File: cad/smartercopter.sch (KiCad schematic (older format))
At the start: 26 parts, among them P1 CONN_5, U1 CC2541, X1 32Mhz

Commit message: everything has a footprint
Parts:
- P1: footprint (none) -> Pin_Arrays:pin_array_1x05
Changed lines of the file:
@@
 F 0 "P1" H 5900 5650 50  0000 C CNN
 F 1 "CONN_5" V 6000 5350 50  0000 C CNN
-F 2 "" H 5900 5350 60  0001 C CNN
+F 2 "Pin_Arrays:pin_array_1x05" H 5900 5350 60  0001 C CNN
 F 3 "" H 5900 5350 60  0000 C CNN
 	1    5900 5350

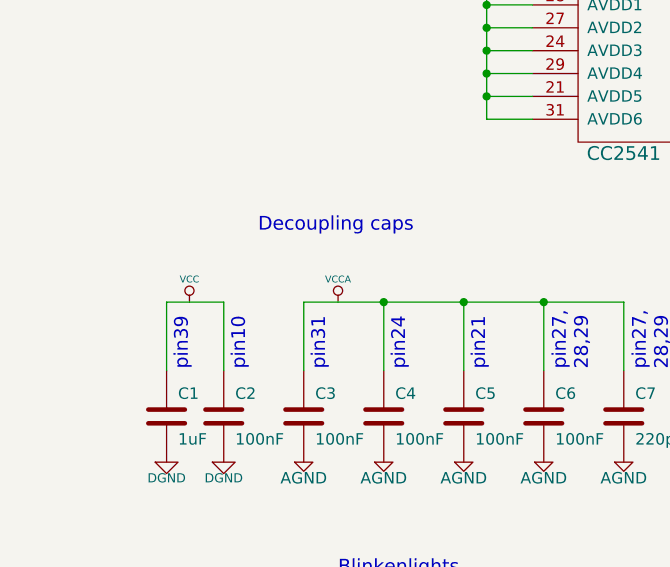
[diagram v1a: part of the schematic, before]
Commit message: found out decoupling caps are not connected in the net
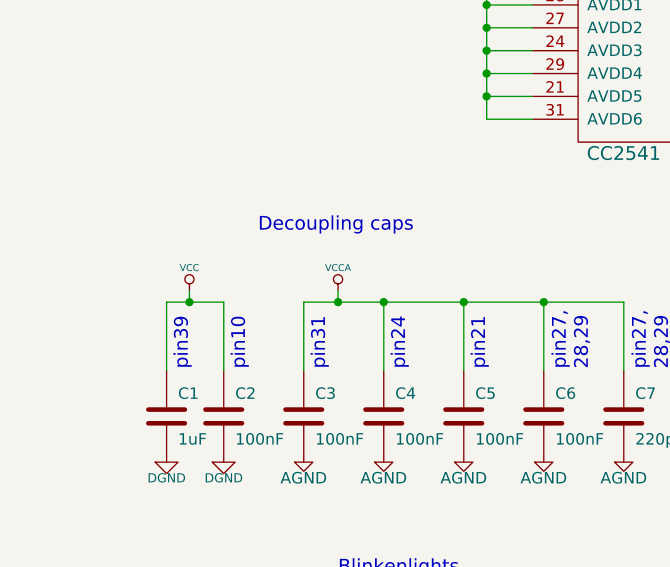
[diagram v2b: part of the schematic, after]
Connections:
- wire segments 104 -> 106

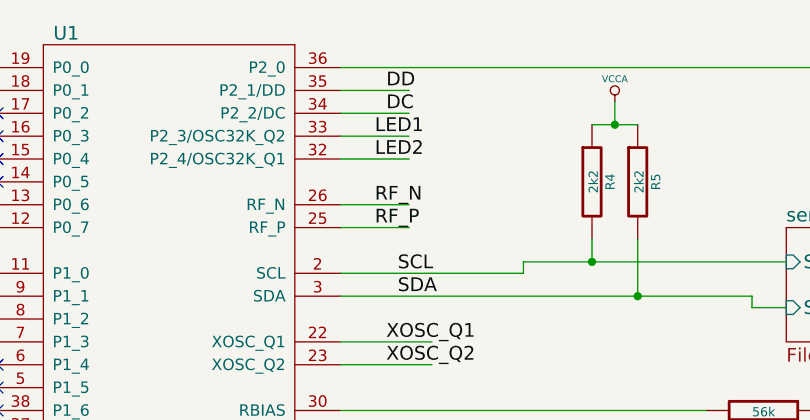
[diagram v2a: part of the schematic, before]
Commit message: components packed closer
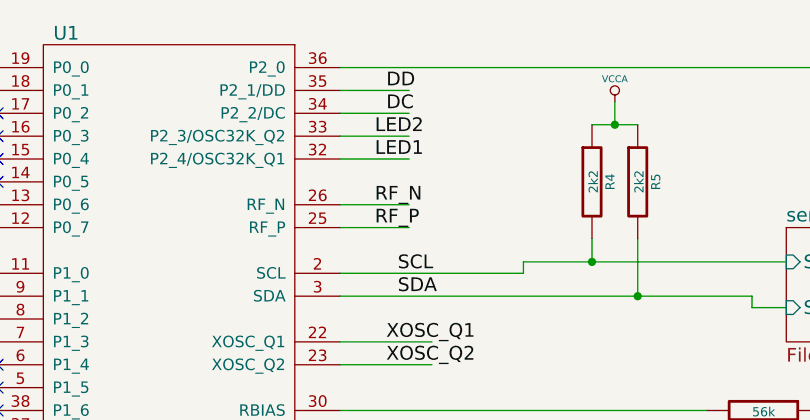
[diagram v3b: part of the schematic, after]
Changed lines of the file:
@@
 DC
 Text Label 5000 1600 0    60   ~ 0
+LED2
+Text Label 5000 1700 0    60   ~ 0
 LED1
-Text Label 5000 1700 0    60   ~ 0
-LED2
 $Comp
 L R R1

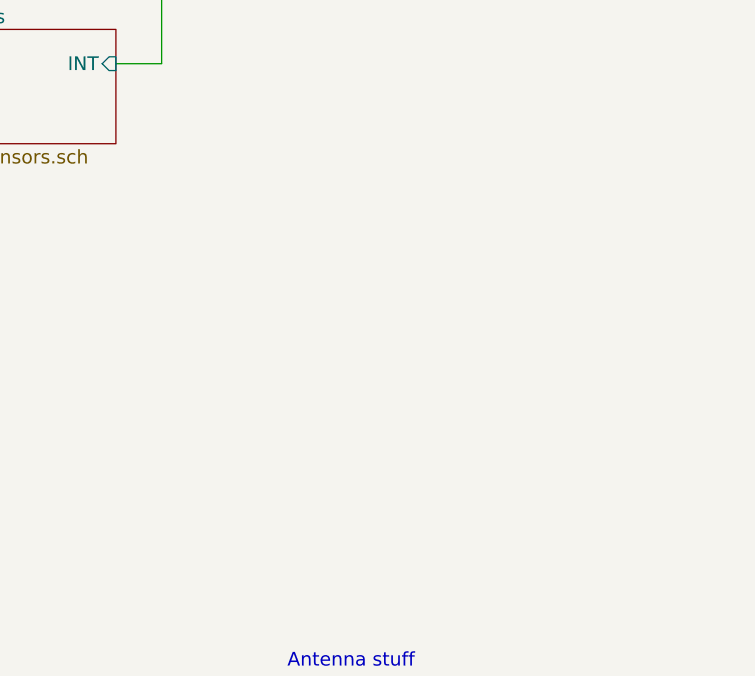
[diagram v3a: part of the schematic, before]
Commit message: added board outline
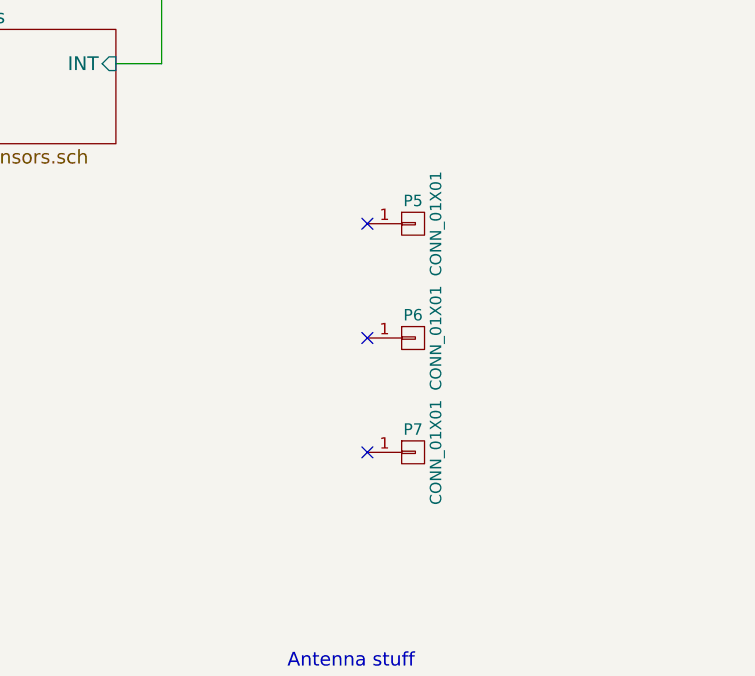
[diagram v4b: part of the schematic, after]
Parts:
- added P5, P6, P7: CONN_01X01, Mounting_Holes:MountingHole_3mm, symbol CONN_01X01
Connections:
- no-connect marks 8 -> 11
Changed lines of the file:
@@
 	2500 4900 2500 4950
 Connection ~ 2500 4950
+$Comp
+L CONN_01X01 P5
+U 1 1 5499BF7C
+P 8900 2850
+F 0 "P5" H 8900 2950 50  0000 C CNN
+F 1 "CONN_01X01" V 9000 2850 50  0000 C CNN
+F 2 "Mounting_Holes:MountingHole_3mm" H 8900 2850 60  0001 C CNN
+F 3 "" H 8900 2850 60  0000 C CNN
+	1    8900 2850
+	1    0    0    -1
+$EndComp
+$Comp
+L CONN_01X01 P6
+U 1 1 5499BFFA
+P 8900 3350
+F 0 "P6" H 8900 3450 50  0000 C CNN
+F 1 "CONN_01X01" V 9000 3350 50  0000 C CNN
+F 2 "Mounting_Holes:MountingHole_3mm" H 8900 3350 60  0001 C CNN
+F 3 "" H 8900 3350 60  0000 C CNN
+	1    8900 3350
+	1    0    0    -1
+$EndComp
+$Comp
+L CONN_01X01 P7
+U 1 1 5499C075
+P 8900 3850
+F 0 "P7" H 8900 3950 50  0000 C CNN
+F 1 "CONN_01X01" V 9000 3850 50  0000 C CNN
+F 2 "Mounting_Holes:MountingHole_3mm" H 8900 3850 60  0001 C CNN
+F 3 "" H 8900 3850 60  0000 C CNN
+	1    8900 3850
+	1    0    0    -1
+$EndComp
+NoConn ~ 8700 2850
+NoConn ~ 8700 3350
+NoConn ~ 8700 3850
 $EndSCHEMATC

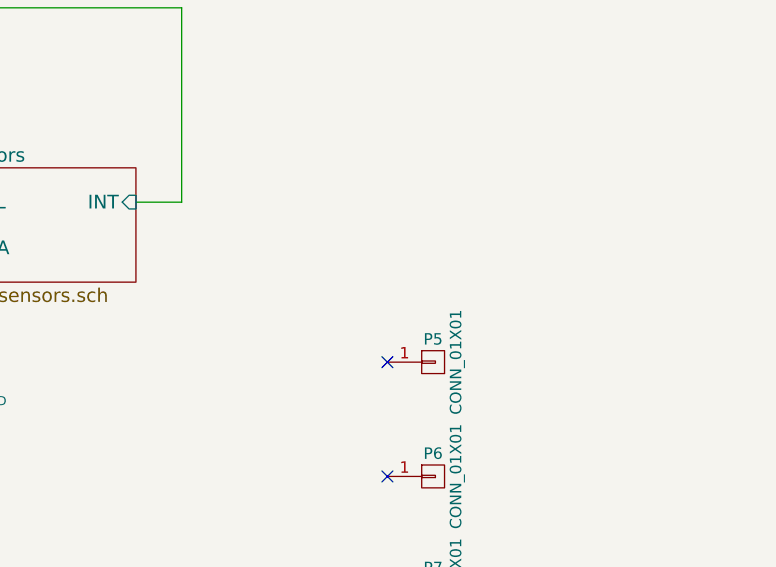
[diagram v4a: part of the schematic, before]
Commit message: made motor pads single to save space
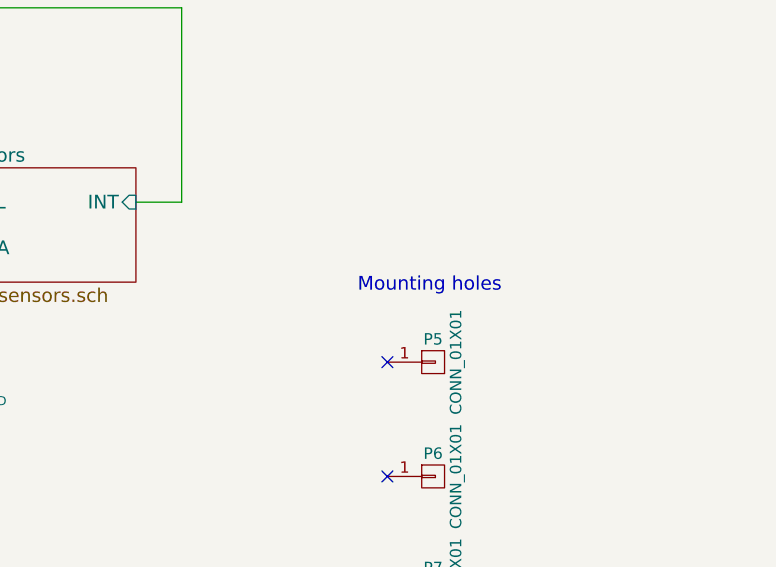
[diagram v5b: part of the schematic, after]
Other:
- note added: "Mounting holes"
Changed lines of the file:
@@
 NoConn ~ 8700 3350
 NoConn ~ 8700 3850
+Text Notes 9200 2550 2    60   ~ 0
+Mounting holes
 $EndSCHEMATC

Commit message: progress check in
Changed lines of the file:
@@
 DC
 Text Label 5000 1600 0    60   ~ 0
+LED1
+Text Label 5000 1700 0    60   ~ 0
 LED2
-Text Label 5000 1700 0    60   ~ 0
-LED1
 $Comp
 L R R1

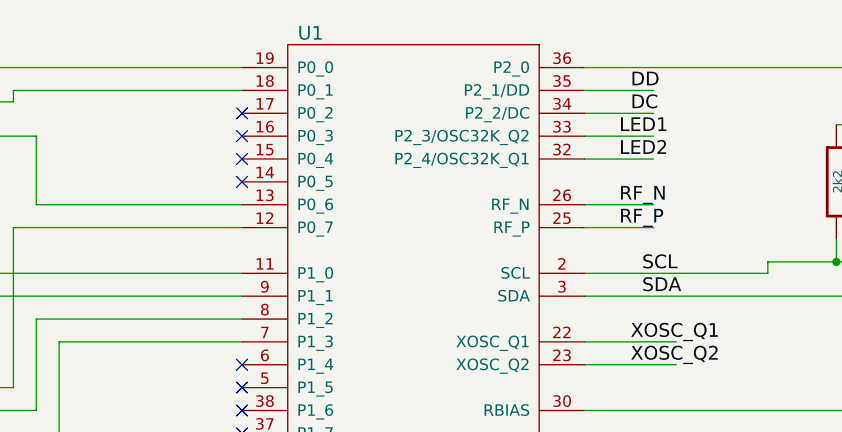
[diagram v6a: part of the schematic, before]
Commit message: everything routed
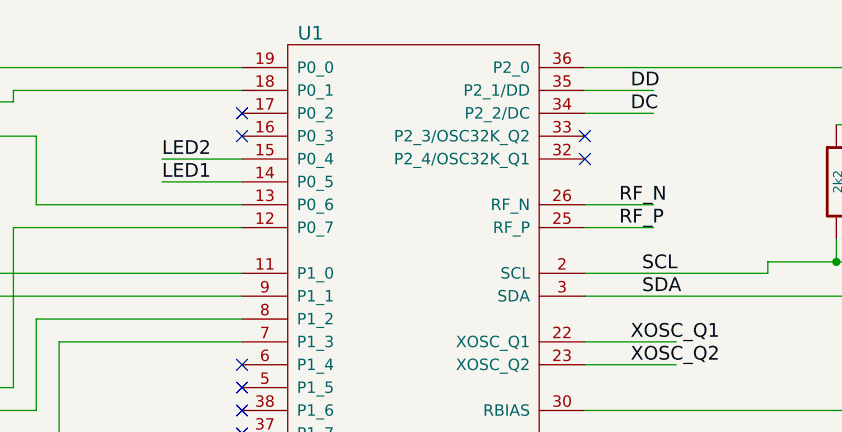
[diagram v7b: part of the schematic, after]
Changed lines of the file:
@@
 Text Label 5050 1500 0    60   ~ 0
 DC
-Text Label 5000 1600 0    60   ~ 0
-LED1
-Text Label 5000 1700 0    60   ~ 0
-LED2
 $Comp
 L R R1
@@
 NoConn ~ 3350 1500
 NoConn ~ 3350 1600
-NoConn ~ 3350 1700
-NoConn ~ 3350 1800
 NoConn ~ 3350 2600
 NoConn ~ 3350 2700
@@
 	2450 1900 3350 1900
 Wire Wire Line
-	4850 1600 5150 1600
-Wire Wire Line
-	5150 1700 4850 1700
-Wire Wire Line
 	3150 6550 3350 6550
 Wire Wire Line
@@
 Text Notes 9200 2550 2    60   ~ 0
 Mounting holes
+Wire Wire Line
+	3350 1800 3000 1800
+Text Label 3000 1800 0    60   ~ 0
+LED1
+Wire Wire Line
+	3350 1700 3000 1700
+Text Label 3000 1700 0    60   ~ 0
+LED2
+NoConn ~ 4850 1600
+NoConn ~ 4850 1700
 $EndSCHEMATC

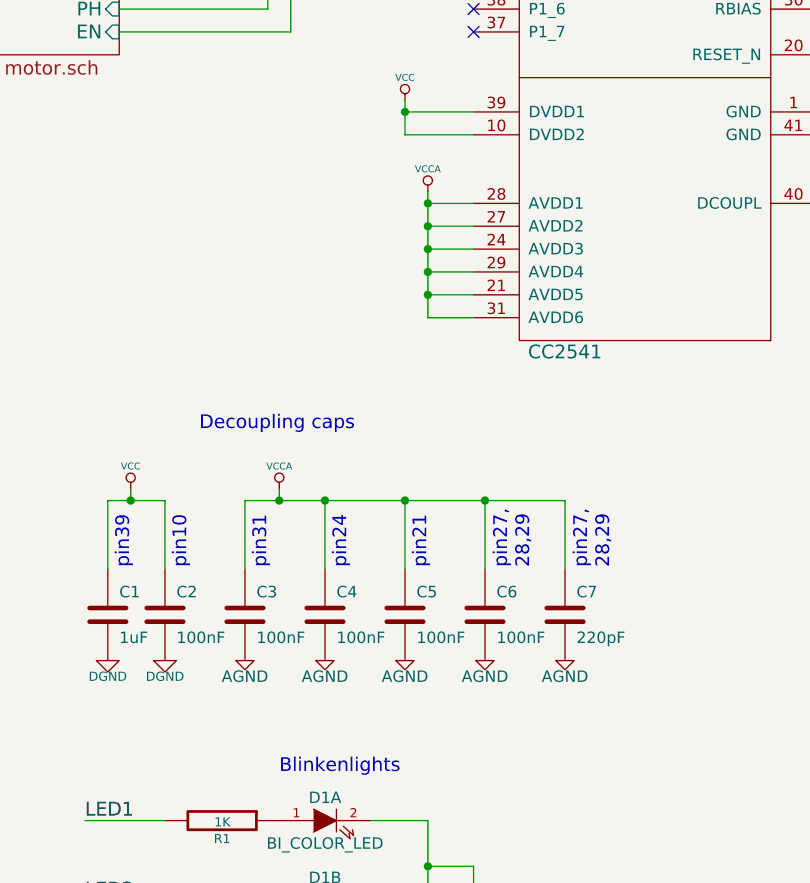
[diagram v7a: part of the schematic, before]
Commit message: double checking qfn-40 footprint
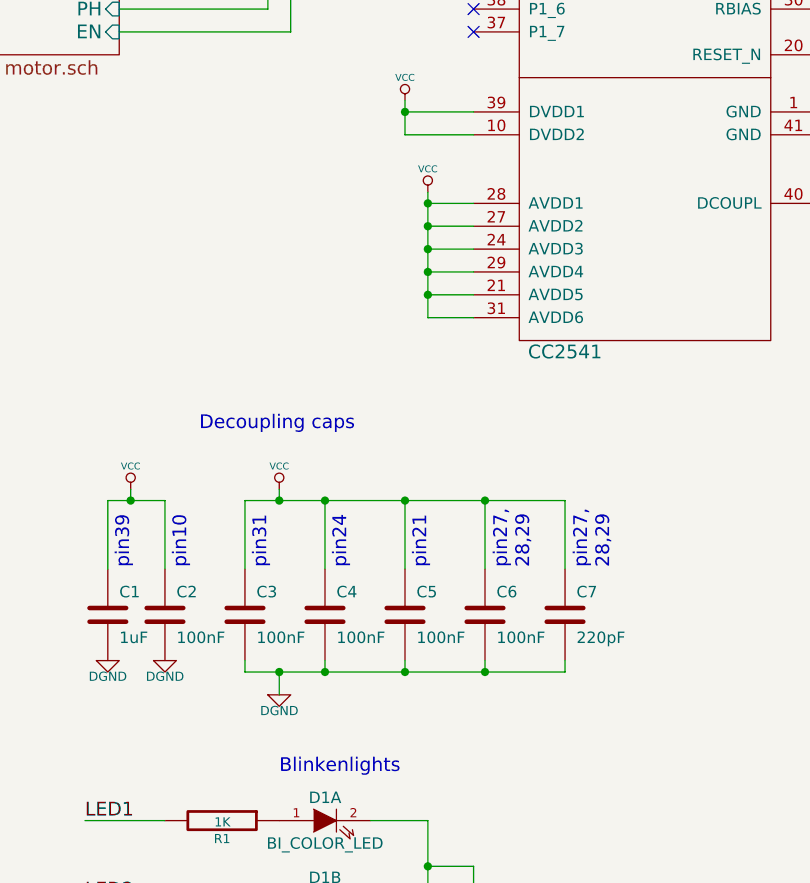
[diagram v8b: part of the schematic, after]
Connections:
- net labels removed: AGND
- wire segments 106 -> 113
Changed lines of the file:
@@
-$EndComp
-$Comp
-L VCCA #PWR01
-U 1 1 548BD9A0
-P 3150 3600
-F 0 "#PWR01" H 3150 3700 30  0001 C CNN
-F 1 "VCCA" H 3150 3700 30  0000 C CNN
-F 2 "" H 3150 3600 60  0000 C CNN
-F 3 "" H 3150 3600 60  0000 C CNN
-	1    3150 3600
-	1    0    0    -1
 $EndComp
 $Comp
@@
 Text Notes 3950 5250 1    60   ~ 0
 pin27,\n28,29
-$Comp
-L AGND #PWR011
-U 1 1 548D5DE4
-P 2350 5650
-F 0 "#PWR011" H 2350 5650 40  0001 C CNN
-F 1 "AGND" H 2350 5580 50  0000 C CNN
-F 2 "" H 2350 5650 60  0000 C CNN
-F 3 "" H 2350 5650 60  0000 C CNN
-	1    2350 5650
-	1    0    0    -1
-$EndComp
-$Comp
-L AGND #PWR012
-U 1 1 548D5E16
-P 2700 5650
-F 0 "#PWR012" H 2700 5650 40  0001 C CNN
-F 1 "AGND" H 2700 5580 50  0000 C CNN
-F 2 "" H 2700 5650 60  0000 C CNN
-F 3 "" H 2700 5650 60  0000 C CNN
-	1    2700 5650
-	1    0    0    -1
-$EndComp
-$Comp
-L AGND #PWR013
-U 1 1 548D5E48
-P 3050 5650
-F 0 "#PWR013" H 3050 5650 40  0001 C CNN
-F 1 "AGND" H 3050 5580 50  0000 C CNN
-F 2 "" H 3050 5650 60  0000 C CNN
-F 3 "" H 3050 5650 60  0000 C CNN
-	1    3050 5650
-	1    0    0    -1
-$EndComp
-$Comp
-L AGND #PWR014
-U 1 1 548D5E98
-P 3400 5650
-F 0 "#PWR014" H 3400 5650 40  0001 C CNN
-F 1 "AGND" H 3400 5580 50  0000 C CNN
-F 2 "" H 3400 5650 60  0000 C CNN
-F 3 "" H 3400 5650 60  0000 C CNN
-	1    3400 5650
-	1    0    0    -1
-$EndComp
-$Comp
-L AGND #PWR015
-U 1 1 548D5ECA
-P 3750 5650
-F 0 "#PWR015" H 3750 5650 40  0001 C CNN
-F 1 "AGND" H 3750 5580 50  0000 C CNN
-F 2 "" H 3750 5650 60  0000 C CNN
-F 3 "" H 3750 5650 60  0000 C CNN
-	1    3750 5650
-	1    0    0    -1
-$EndComp
-$Comp
-L VCCA #PWR016
-U 1 1 548D65F8
-P 2500 4900
-F 0 "#PWR016" H 2500 5000 30  0001 C CNN
-F 1 "VCCA" H 2500 5000 30  0000 C CNN
-F 2 "" H 2500 4900 60  0000 C CNN
-F 3 "" H 2500 4900 60  0000 C CNN
-	1    2500 4900
-	1    0    0    -1
-$EndComp
 $Sheet
 S 1250 1200 550  500
@@
 NoConn ~ 4850 1600
 NoConn ~ 4850 1700
+$Comp
+L VCC #PWR?
+U 1 1 54AB4FF1
+P 3150 3600
+F 0 "#PWR?" H 3150 3700 30  0001 C CNN
+F 1 "VCC" H 3150 3700 30  0000 C CNN
+F 2 "" H 3150 3600 60  0000 C CNN
+F 3 "" H 3150 3600 60  0000 C CNN
+	1    3150 3600
+	1    0    0    -1
+$EndComp
+$Comp
+L VCC #PWR?
+U 1 1 54AB73FC
+P 2500 4900
+F 0 "#PWR?" H 2500 5000 30  0001 C CNN
+F 1 "VCC" H 2500 5000 30  0000 C CNN
+F 2 "" H 2500 4900 60  0000 C CNN
+F 3 "" H 2500 4900 60  0000 C CNN
+	1    2500 4900
+	1    0    0    -1
+$EndComp
+Wire Wire Line
+	2350 5650 2350 5700
+Wire Wire Line
+	2350 5700 3750 5700
+Wire Wire Line
+	3750 5700 3750 5650
+Wire Wire Line
+	3400 5650 3400 5700
+Connection ~ 3400 5700
+Wire Wire Line
+	3050 5650 3050 5700
+Connection ~ 3050 5700
+Wire Wire Line
+	2700 5650 2700 5700
+Connection ~ 2700 5700
+$Comp
+L DGND #PWR?
+U 1 1 54AB843E
+P 2500 5800
+F 0 "#PWR?" H 2500 5800 40  0001 C CNN
+F 1 "DGND" H 2500 5730 40  0000 C CNN
+F 2 "" H 2500 5800 60  0000 C CNN
+F 3 "" H 2500 5800 60  0000 C CNN
+	1    2500 5800
+	1    0    0    -1
+$EndComp
+Wire Wire Line
+	2500 5800 2500 5700
+Connection ~ 2500 5700
 $EndSCHEMATC
